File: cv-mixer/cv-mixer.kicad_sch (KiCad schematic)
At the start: 45 parts, among them J1 Input A1, J10 Pot, J11 Input B3, J12 Pot, J13 Pot, J14 Output A, J15 Pot, J16 Output B, J17 AudioJack4, J18 Power, J19 Power, J2 Pot, J3 Input A2, J4 Pot, J5 Input A3, J6 Pot, J7 Input B1, J8 Pot, J9 Input B2, SW1 Mono/Stereo, U1 TL072

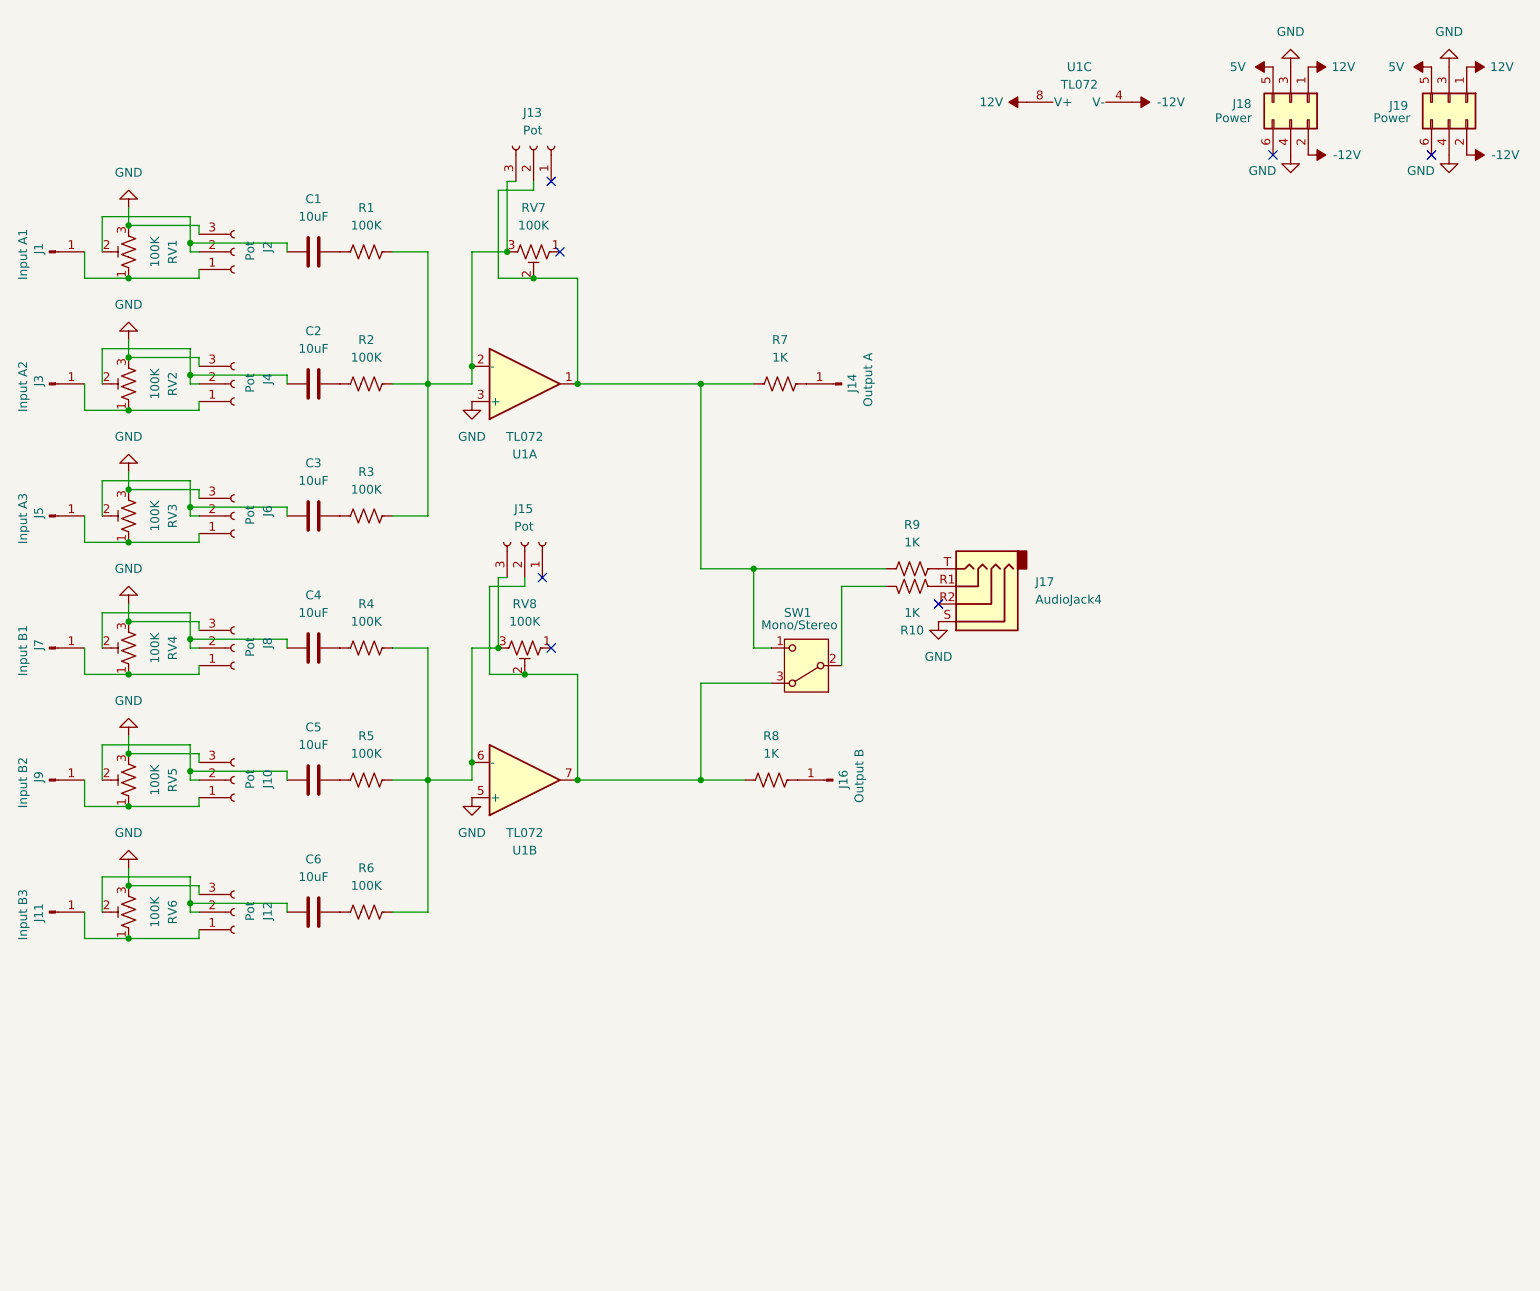
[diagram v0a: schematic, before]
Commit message: Add cv mixer
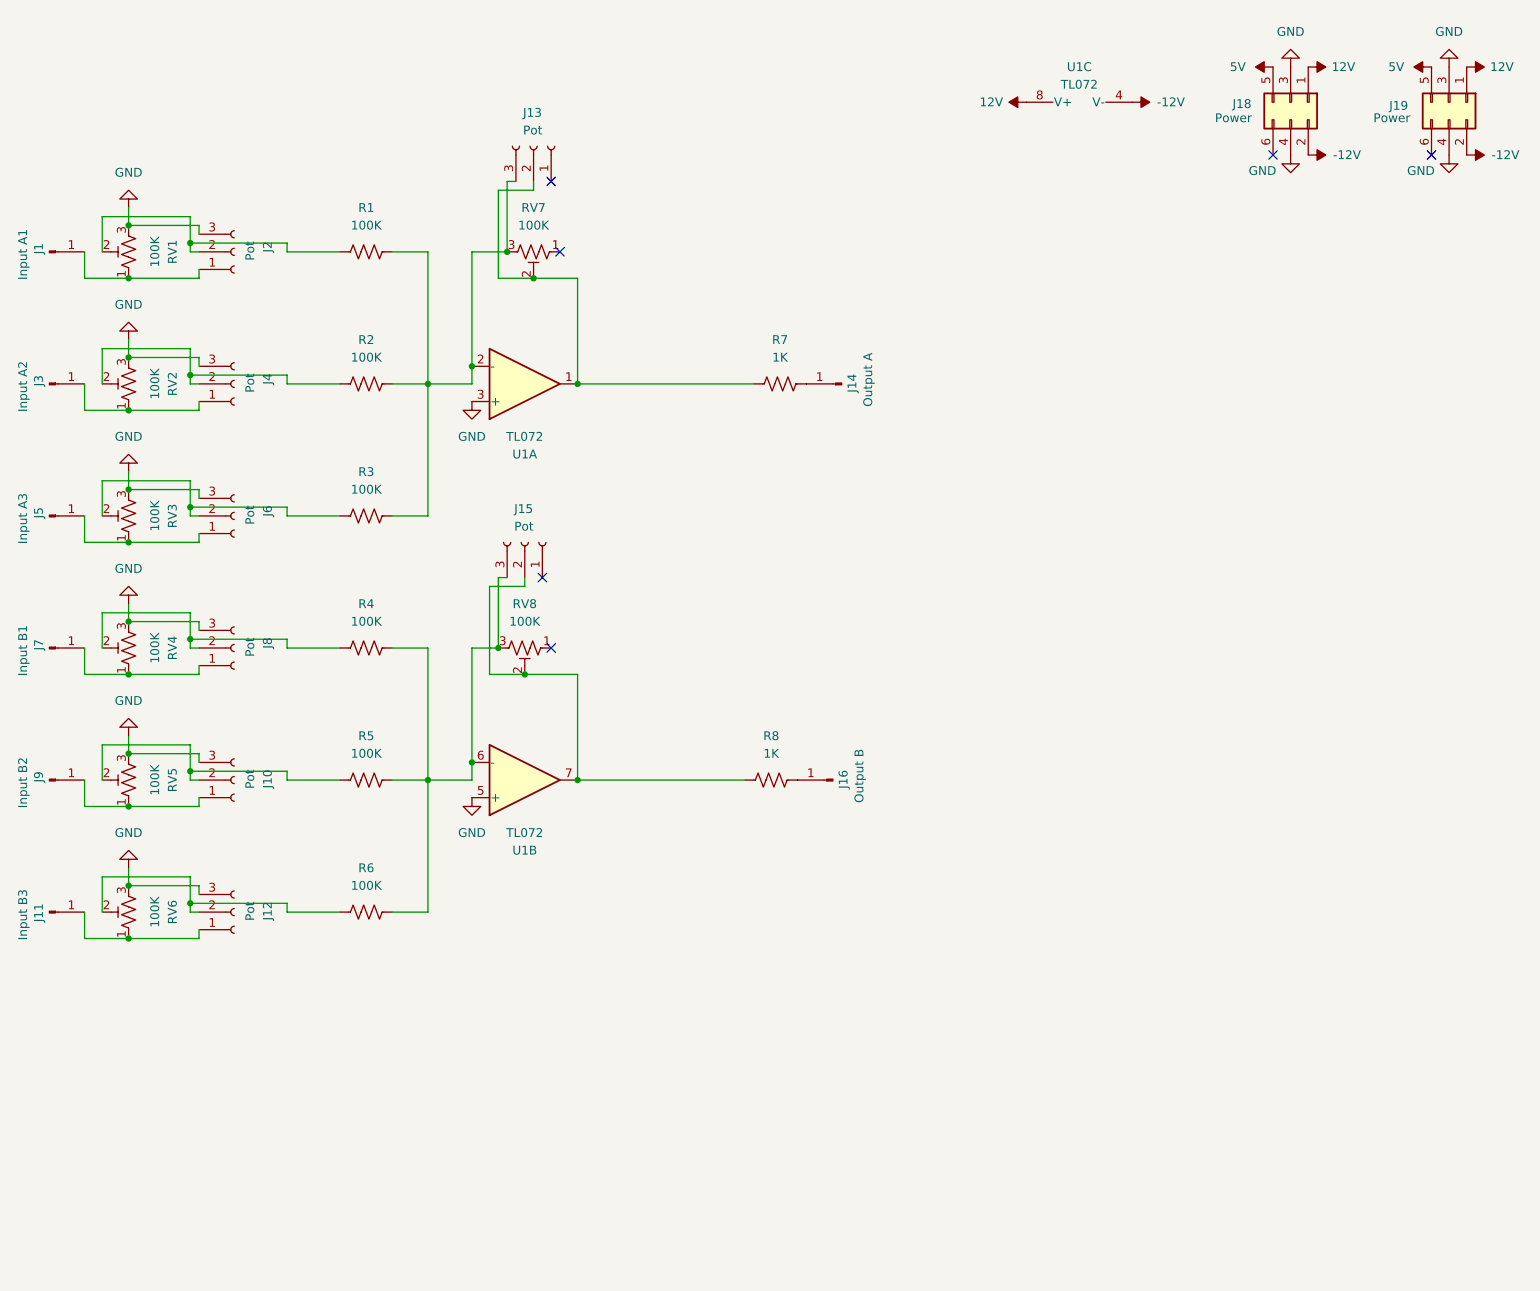
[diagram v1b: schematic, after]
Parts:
- removed C1, C2, C3, C4, C5, C6: 10uF, Capacitor_THT:C_Disc_D4.3mm_W1.9mm_P5.00mm, symbol Device:C
- removed J17: AudioJack4, modular2:audio jack breakout, symbol Connector_Audio:AudioJack4
- removed R10, R9: 1K, Resistor_THT:R_Axial_DIN0207_L6.3mm_D2.5mm_P10.16mm_Horizontal, symbol Device:R_US
- removed SW1: Mono/Stereo, modular2:switch1, symbol Switch:SW_Nidec_CAS-120A1
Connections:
- net at J2.2 (Pin_2), RV1.2: now also R1.1
- net at J12.2 (Pin_2), RV6.2: now also R6.1
- net at R2.1: now also J4.2 (Pin_2), RV2.2
- net at J10.2 (Pin_2), RV5.2: now also R5.1
- net at R3.1: now also J6.2 (Pin_2), RV3.2
- net at R4.1: now also J8.2 (Pin_2), RV4.2
- no-connect marks 7 -> 6

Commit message: Various improvements
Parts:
- added C1, C2: 100nF, Capacitor_THT:C_Disc_D4.3mm_W1.9mm_P5.00mm, symbol Device:C
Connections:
- net -12V: now also C2.2
- net 12V: now also C1.2
- net GND: now also C1.1, C2.1

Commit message: Various fixes
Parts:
- added J17: Power, Connector_IDC:IDC-Header_2x03_P2.54mm_Vertical, symbol Connector_Generic:Conn_02x03_Odd_Even
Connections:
- net -12V: now also J17.2 (Pin_2)
- net 12V: now also J17.1 (Pin_1)
- net 5V: now also J17.5 (Pin_5)
- net GND: now also J10.1 (Pin_1), J12.1 (Pin_1), J2.1 (Pin_1), J4.1 (Pin_1), J6.1 (Pin_1), J8.1 (Pin_1), RV1.1, RV2.1, RV3.1, RV4.1, RV5.1, RV6.1, J17.3 (Pin_3), J17.4 (Pin_4); no longer J10.3 (Pin_3), J12.3 (Pin_3), J2.3 (Pin_3), J4.3 (Pin_3), J6.3 (Pin_3), J8.3 (Pin_3), RV1.3, RV2.3, RV3.3, RV4.3, RV5.3, RV6.3
- net at R1.2, R2.2, R3.2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: now also J13.1 (Pin_1), RV7.1; no longer J13.3 (Pin_3), RV7.3
- net at J15.1 (Pin_1): now also R4.2, R5.2, R6.2, RV8.1, U1.6 (-)
- new net: J1.1 (Pin_1), J2.3 (Pin_3), RV1.3
- new net: J3.1 (Pin_1), J4.3 (Pin_3), RV2.3
- new net: J5.1 (Pin_1), J6.3 (Pin_3), RV3.3
- new net: J7.1 (Pin_1), J8.3 (Pin_3), RV4.3
- new net: J10.3 (Pin_3), J9.1 (Pin_1), RV5.3
- new net: J11.1 (Pin_1), J12.3 (Pin_3), RV6.3
- now unconnected: J15.3 (Pin_3), RV8.3
- no-connect marks 6 -> 7
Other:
- moved on the sheet: C1, C2, J13, J15, J18, J19, RV1, RV2, RV3, RV4, RV5, RV6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

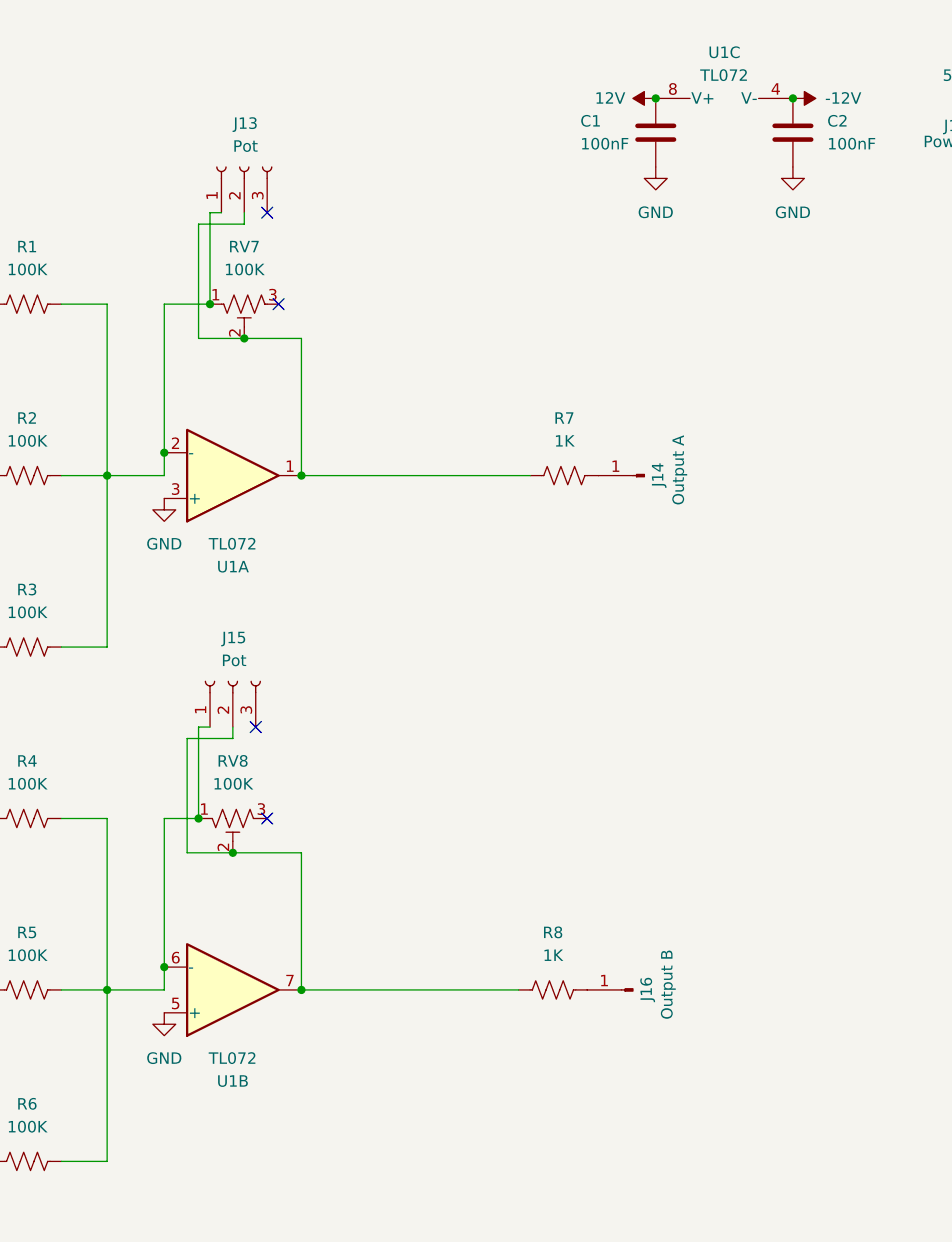
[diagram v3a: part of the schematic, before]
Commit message: Fix bug where cv mixer output was flipped
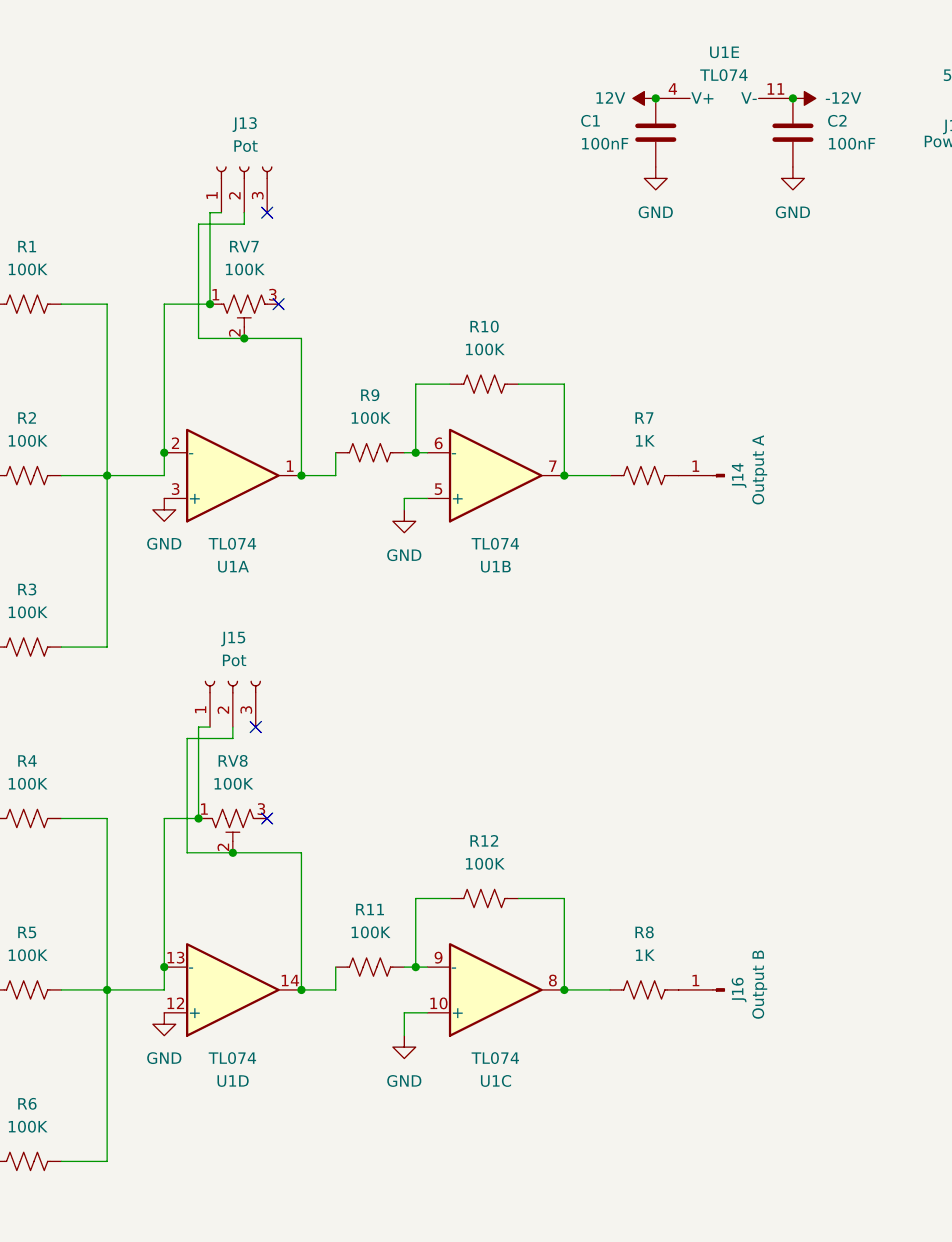
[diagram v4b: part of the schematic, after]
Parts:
- removed U1: TL072, Package_DIP:DIP-8_W7.62mm_Socket, symbol Amplifier_Operational:TL072
- added R10, R11, R12, R9: 100K, Resistor_THT:R_Axial_DIN0207_L6.3mm_D2.5mm_P10.16mm_Horizontal, symbol Device:R_US
- added U1: TL074, Package_DIP:DIP-14_W7.62mm_Socket, symbol Amplifier_Operational:TL074
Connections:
- net -12V: now also U1.11 (V-)
- net 12V: now also U1.4 (V+)
- net GND: now also U1.10 (+), U1.12 (+), U1.3 (+), U1.5 (+)
- net at J13.1 (Pin_1), R1.2, R2.2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: now also U1.2 (-)
- net at J15.1 (Pin_1), R4.2, R5.2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: now also U1.13 (-)
- net at J15.2 (Pin_2), RV8.2: now also R11.1, U1.14; no longer R8.1
- net at J13.2 (Pin_2), RV7.2: now also R9.1, U1.1; no longer R7.1
- new net: R11.2, R12.1, U1.9 (-)
- new net: R12.2, R8.1, U1.8
- new net: R10.2, R7.1, U1.7
- new net: R10.1, R9.2, U1.6 (-)
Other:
- moved on the sheet: J14, J16, R7, R8
